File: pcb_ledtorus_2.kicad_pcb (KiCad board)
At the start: 4 copper layers, 199 x 199 mm, 273 parts, among them P1 CONN_02X04, P2 CONN_6, P3 MICRO-SD, P4 CONN_2, P5 KNUSB, P6 CONN_12, U1 STM32F46X_LQFP176, U10 TLC5955, U11 TLC5955, U12 TLC5955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

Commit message: Couple small tweaks, 3d shapes.
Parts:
- X1: footprint knielsenlib_old:2-SOJ -> knielsenlib:2-SOJ
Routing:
- net /LEDs/sclk2: track 0.00 -> 34.0 mm
- net /LEDs/gsclk2: track 0.00 -> 33.9 mm
- net Net-(U6-Pad28): track 0.00 -> 18.0 mm
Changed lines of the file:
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@@
   (general
     (links 1069)
-    (no_connects 979)
+    (no_connects 976)
     (area 50.449846 50.424999 249.550154 249.575001)
     (thickness 0.8)
     (drawings 85)
-    (tracks 3)
+    (tracks 14)
     (zones 0)
     (modules 273)
@@
     (uvia_drill 0.127)
   )
+  (module knielsenlib:TO-252-3 (layer B.Cu)
+    (at 127.286 215.22072)
+    (descr "TO-252-3 (also PFM) package")
+    (fp_text reference U3 (at 0 7.69874) (layer B.SilkS)
+      (effects (font (thickness 0.3048)) (justify mirror))
+    )
+    (fp_text value LP38691 (at 0 -5.99948) (layer B.SilkS)
+      (effects (font (thickness 0.3048)) (justify mirror))
+    )
+    (pad 1 smd rect (at -2.286 -3.22072) (size 1.30048 1.69926) (layers B.Cu B.Paste B.Mask)
+      (net 3 +3V3))
+    (pad 3 smd rect (at 2.286 -3.22072) (size 1.30048 1.69926) (layers B.Cu B.Paste B.Mask)
+      (net 6 +5V))
+    (pad 2 smd rect (at 0 3.22072) (size 5.4991 5.69976) (layers B.Cu B.Paste B.Mask)
+      (net 2 GND))
+    (model TO_SOT_Packages_SMD.3dshapes/TO-252-2Lead.wrl
+      (at (xyz 0 -0.118 0))
+      (scale (xyz 1 1 1))
+      (rotate (xyz 0 0 0))
+    )
+  )
+  (module knielsenlib:RGB_0603 (layer F.Cu)
+    (at 199.734424 109.343679 90)
+    (descr "RGB led, 0603")
+    (fp_text reference LD35 (at 0 -1.15 90) (layer F.SilkS)
+      (effects (font (size 0.20066 0.20066) (thickness 0.04064)))
+    )
+    (fp_text value RGB_LED_SMALL (at 0 1.15 90) (layer F.SilkS) hide
+      (effects (font (size 0.20066 0.20066) (thickness 0.04064)))
+    )
+    (fp_line (start 1.75 -0.1) (end 1.75 0.1) (layer F.SilkS) (width 0.15))
+    (fp_line (start -0.8 -0.55) (end -0.8 -0.75) (layer F.SilkS) (width 0.15))
+    (fp_line (start -0.8 0.25) (end -0.8 -0.25) (layer F.SilkS) (width 0.15))
+    (fp_line (start -0.8 0.75) (end -0.8 0.55) (layer F.SilkS) (width 0.15))
+    (fp_line (start 0.8 0.55) (end 0.8 0.75) (layer F.SilkS) (width 0.15))
+    (fp_line (start 0.8 -0.25) (end 0.8 0.25) (layer F.SilkS) (width 0.15))
+    (fp_line (start 0.8 -0.75) (end 0.8 -0.55) (layer F.SilkS) (width 0.15))
+    (fp_arc (start 0.95 -0.4) (end 0.8 -0.25) (angle 90) (layer F.SilkS) (width 0.15))
+    (fp_arc (start 0.95 0.4) (end 0.8 0.55) (angle 90) (layer F.SilkS) (width 0.15))
+    (fp_arc (start -0.95 0.4) (end -0.8 0.25) (angle 90) (layer F.SilkS) (width 0.15))
+    (fp_arc (start -0.95 -0.4) (end -0.8 -0.55) (angle 90) (layer F.SilkS) (width 0.15))
+    (fp_line (start -0.8 -0.75) (end 0.8 -0.75) (layer F.SilkS) (width 0.15))
+    (fp_line (start 0.8 0.75) (end -0.8 0.75) (layer F.SilkS) (width 0.15))
+    (pad 4 smd rect (at 0.875 -0.4625 90) (size 1.05 0.575) (layers F.Cu F.Paste F.Mask)
+      (net 118 /LEDs/led35b))
+    (pad 1 smd rect (at 0.875 0.4625 90) (size 1.05 0.575) (layers F.Cu F.Paste F.Mask)
+      (net 6 +5V))
+    (pad 2 smd rect (at -0.875 0.4625 90) (size 1.05 0.575) (layers F.Cu F.Paste F.Mask)
+      (net 119 /LEDs/led35r))
+    (pad 3 smd rect (at -0.875 -0.4625 90) (size 1.05 0.575) (layers F.Cu F.Paste F.Mask)
+      (net 120 /LEDs/led35g))
+    (model walter/smd_leds/led_0603.wrl
+      (at (xyz 0 0 0))
+      (scale (xyz 1 1 1))
+      (rotate (xyz 0 0 0))
+    )
+  )
   (module knielsenlib:SWITCH_FSMJSMA (layer B.Cu)
     (at 152.5 179.04914)
@@
   )
   (module knielsenlib:RGB_0603 (layer F.Cu)
-    (at 199.734424 109.343679 90)
-    (descr "RGB led, 0603")
-    (fp_text reference LD35 (at 0 -1.15 90) (layer F.SilkS)
-      (effects (font (size 0.20066 0.20066) (thickness 0.04064)))
-    )
-    (fp_text value RGB_LED_SMALL (at 0 1.15 90) (layer F.SilkS) hide
-      (effects (font (size 0.20066 0.20066) (thickness 0.04064)))
-    )
-    (fp_line (start 1.75 -0.1) (end 1.75 0.1) (layer F.SilkS) (width 0.15))
-    (fp_line (start -0.8 -0.55) (end -0.8 -0.75) (layer F.SilkS) (width 0.15))
-    (fp_line (start -0.8 0.25) (end -0.8 -0.25) (layer F.SilkS) (width 0.15))
-    (fp_line (start -0.8 0.75) (end -0.8 0.55) (layer F.SilkS) (width 0.15))
-    (fp_line (start 0.8 0.55) (end 0.8 0.75) (layer F.SilkS) (width 0.15))
-    (fp_line (start 0.8 -0.25) (end 0.8 0.25) (layer F.SilkS) (width 0.15))
-    (fp_line (start 0.8 -0.75) (end 0.8 -0.55) (layer F.SilkS) (width 0.15))
-    (fp_arc (start 0.95 -0.4) (end 0.8 -0.25) (angle 90) (layer F.SilkS) (width 0.15))
-    (fp_arc (start 0.95 0.4) (end 0.8 0.55) (angle 90) (layer F.SilkS) (width 0.15))
-    (fp_arc (start -0.95 0.4) (end -0.8 0.25) (angle 90) (layer F.SilkS) (width 0.15))
-    (fp_arc (start -0.95 -0.4) (end -0.8 -0.55) (angle 90) (layer F.SilkS) (width 0.15))
-    (fp_line (start -0.8 -0.75) (end 0.8 -0.75) (layer F.SilkS) (width 0.15))
-    (fp_line (start 0.8 0.75) (end -0.8 0.75) (layer F.SilkS) (width 0.15))
-    (pad 4 smd rect (at 0.875 -0.4625 90) (size 1.05 0.575) (layers F.Cu F.Paste F.Mask)
-      (net 118 /LEDs/led35b))
-    (pad 1 smd rect (at 0.875 0.4625 90) (size 1.05 0.575) (layers F.Cu F.Paste F.Mask)
-      (net 6 +5V))
-    (pad 2 smd rect (at -0.875 0.4625 90) (size 1.05 0.575) (layers F.Cu F.Paste F.Mask)
-      (net 119 /LEDs/led35r))
-    (pad 3 smd rect (at -0.875 -0.4625 90) (size 1.05 0.575) (layers F.Cu F.Paste F.Mask)
-      (net 120 /LEDs/led35g))
-    (model walter/smd_leds/led_0603.wrl
-      (at (xyz 0 0 0))
-      (scale (xyz 1 1 1))
-      (rotate (xyz 0 0 0))
-    )
-  )
-  (module knielsenlib:RGB_0603 (layer F.Cu)
     (at 206.176698 109.343679 90)
     (descr "RGB led, 0603")
@@
     )
   )
-  (module knielsenlib:TO-252-3 (layer B.Cu)
-    (at 127.286 215.22072)
-    (descr "TO-252-3 (also PFM) package")
-    (fp_text reference U3 (at 0 7.69874) (layer B.SilkS)
-      (effects (font (thickness 0.3048)) (justify mirror))
-    )
-    (fp_text value LP38691 (at 0 -5.99948) (layer B.SilkS)
-      (effects (font (thickness 0.3048)) (justify mirror))
-    )
-    (pad 1 smd rect (at -2.286 -3.22072) (size 1.30048 1.69926) (layers B.Cu B.Paste B.Mask)
-      (net 3 +3V3))
-    (pad 3 smd rect (at 2.286 -3.22072) (size 1.30048 1.69926) (layers B.Cu B.Paste B.Mask)
-      (net 6 +5V))
-    (pad 2 smd rect (at 0 3.22072) (size 5.4991 5.69976) (layers B.Cu B.Paste B.Mask)
-      (net 2 GND))
-  )
-  (module knielsenlib_old:2-SOJ (layer B.Cu)
-    (at 104.5 144.4501 90)
-    (descr "Eg. MA-505 crystal")
-    (fp_text reference X1 (at 0 5.00126 90) (layer B.SilkS)
-      (effects (font (thickness 0.3048)) (justify mirror))
-    )
-    (fp_text value MA-505 (at 0 -5.00126 90) (layer B.SilkS)
-      (effects (font (thickness 0.3048)) (justify mirror))
-    )
-    (pad 1 smd rect (at -5.5499 0 90) (size 4.09956 5.6007) (layers B.Cu B.Paste B.Mask)
-      (net 10 /Power/osc_in))
-    (pad 2 smd rect (at 5.5499 0 90) (size 4.09956 5.6007) (layers B.Cu B.Paste B.Mask)
-      (net 11 /Power/osc_out))
-  )
   (module knielsenlib:TLC5955DCA (layer B.Cu)
     (at 163 75)
@@
     )
   )
+  (module knielsenlib:2-SOJ (layer B.Cu)
+    (at 104.5 144.4501 90)
+    (descr "Eg. MA-505 crystal")
+    (fp_text reference X1 (at 0 5.00126 90) (layer B.SilkS)
+      (effects (font (thickness 0.3048)) (justify mirror))
+    )
+    (fp_text value MA-505 (at 0 -5.00126 90) (layer B.SilkS)
+      (effects (font (thickness 0.3048)) (justify mirror))
+    )
+    (pad 1 smd rect (at -5.5499 0 90) (size 4.09956 5.6007) (layers B.Cu B.Paste B.Mask)
+      (net 10 /Power/osc_in))
+    (pad 2 smd rect (at 5.5499 0 90) (size 4.09956 5.6007) (layers B.Cu B.Paste B.Mask)
+      (net 11 /Power/osc_out))
+    (model walter/crystal/crystal_smd_ma-505.wrl
+      (at (xyz 0 0 0))
+      (scale (xyz 1 1 1))
+      (rotate (xyz 0 0 0))
+    )
+  )
   (gr_line (start 214.038448 54.010849) (end 210.571762 50.5) (layer Edge.Cuts) (width 0.15))
   (gr_line (start 217.377214 57.713438) (end 214.038448 54.010849) (layer Edge.Cuts) (width 0.15))
@@
   (segment (start 175.635535 81.364465) (end 175.9 81.1) (width 0.2032) (layer F.Cu) (net 6))
   (via (at 175.9 81.1) (size 0.635) (drill 0.3048) (layers F.Cu B.Cu) (net 6))
+  (segment (start 168.7593 107.1) (end 199.7407 107.1) (width 0.2032) (layer B.Cu) (net 652))
+  (segment (start 199.7407 107.1) (end 200 107.3593) (width 0.2032) (layer B.Cu) (net 652))
+  (segment (start 200 107.3593) (end 200 108.475) (width 0.2032) (layer B.Cu) (net 652))
+  (segment (start 168.5 108.475) (end 168.5 107.3593) (width 0.2032) (layer B.Cu) (net 652))
+  (segment (start 168.5 107.3593) (end 168.7593 107.1) (width 0.2032) (layer B.Cu) (net 652))
+  (segment (start 168.5 101) (end 168.5 102.1157) (width 0.2032) (layer B.Cu) (net 683))
+  (segment (start 168.5 102.1157) (end 168.7843 102.4) (width 0.2032) (layer B.Cu) (net 683))
+  (segment (start 168.7843 102.4) (end 199.7157 102.4) (width 0.2032) (layer B.Cu) (net 683))
+  (segment (start 199.7157 102.4) (end 200 102.1157) (width 0.2032) (layer B.Cu) (net 683))
+  (segment (start 200 102.1157) (end 200 101) (width 0.2032) (layer B.Cu) (net 683))
+  (segment (start 181.5 101) (end 199.5 101) (width 0.2032) (layer B.Cu) (net 738))
   (zone (net 2) (net_name GND) (layer In2.Cu) (hatch edge 0.508)
     (connect_pads (clearance 0.2032))

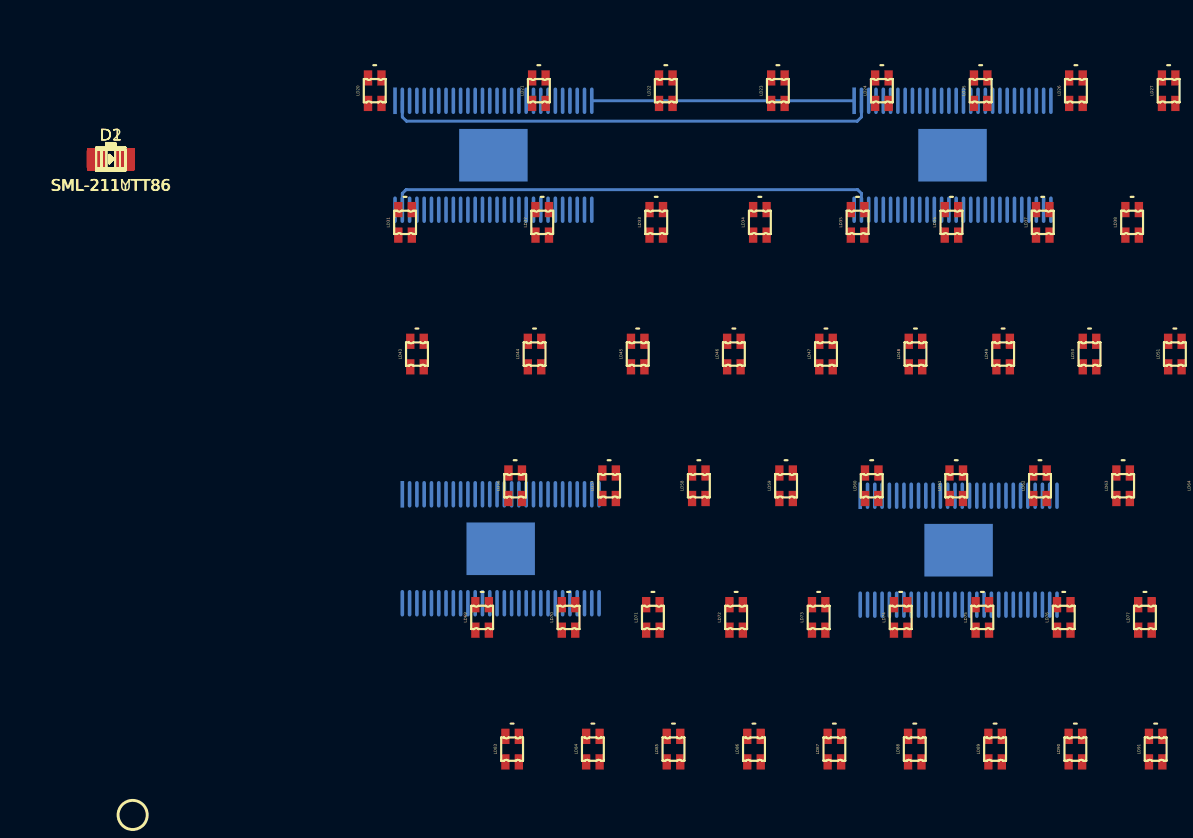
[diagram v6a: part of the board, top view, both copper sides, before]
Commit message: Some experiments with a way to route the LEDs
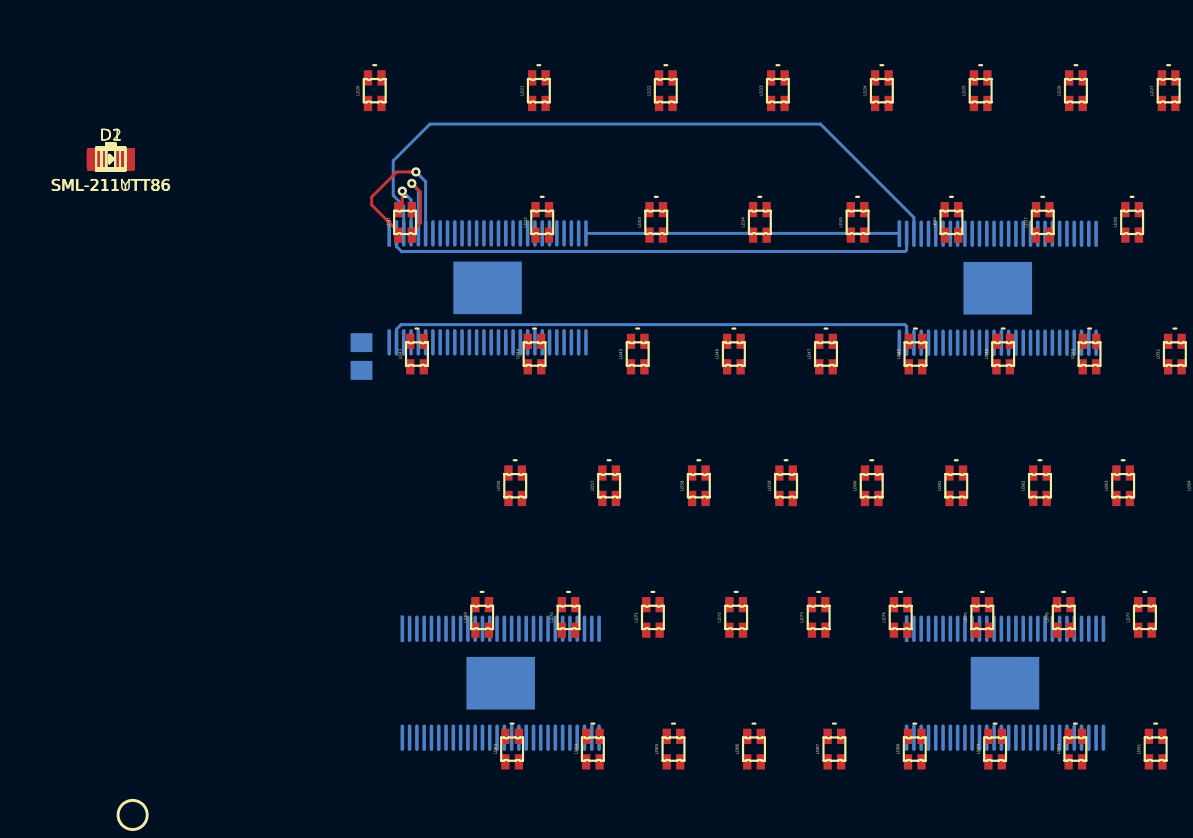
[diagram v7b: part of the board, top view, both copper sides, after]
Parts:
- C36: moved to B.Cu
- moved C36 21.9 mm to (165.7, 118.5), turned to 270 degrees
- moved U9 9.67 mm to (209.8, 141.0)
- moved U7 9.64 mm to (209.3, 113.9)
- moved U8 9.22 mm to (175.2, 141.0)
- moved U6 9.11 mm to (174.3, 113.8)
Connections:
- U5 pad 33: /LEDs/led31g -> /LEDs/led33g
- U5 pad 34: /LEDs/led31r -> /LEDs/led33r
- U5 pad 35: /LEDs/led31b -> /LEDs/led33b
- U6 pad 4: /LEDs/led33b -> /LEDs/led31b
- U6 pad 5: /LEDs/led33r -> /LEDs/led31r
- U6 pad 6: /LEDs/led33g -> /LEDs/led31g
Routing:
- net /LEDs/lat2: track 0.00 -> 45.8 mm
- net /LEDs/led31g: track 0.00 -> 11.6 mm, vias 0 -> 1
- net /LEDs/led31r: track 0.00 -> 7.65 mm, vias 0 -> 1
- net /LEDs/led31b: track 0.00 -> 4.53 mm, vias 0 -> 1
- net Net-(U6-Pad28): track 18.0 -> 21.5 mm
- net /LEDs/gsclk2: track 33.9 -> 37.2 mm
- net /LEDs/sclk2: track 34.0 -> 37.2 mm

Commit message: Intermediate commit
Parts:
- moved U4 7.01 mm to (168.2, 70.3)
- moved U5 4.44 mm to (199.0, 70.3)
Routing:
- net /LEDs/lat3: track 0.00 -> 41.1 mm
- net /LEDs/led96b: track 0.00 -> 37.0 mm, vias 0 -> 1
- net /LEDs/sclk3: track 0.00 -> 36.9 mm
- net /LEDs/gsclk3: track 0.00 -> 36.9 mm
- net /LEDs/led88b: track 0.00 -> 36.1 mm, vias 0 -> 1
- net /LEDs/led96r: track 0.00 -> 35.7 mm, vias 0 -> 1
- net /LEDs/led88r: track 0.00 -> 35.0 mm, vias 0 -> 1
- net /LEDs/led87b: track 0.00 -> 34.5 mm, vias 0 -> 1
- net /LEDs/led87r: track 0.00 -> 33.9 mm, vias 0 -> 1
- net /LEDs/led96g: track 0.00 -> 33.6 mm, vias 0 -> 1
- net /LEDs/led88g: track 0.00 -> 33.1 mm, vias 0 -> 1
- net /LEDs/led87g: track 0.00 -> 31.0 mm, vias 0 -> 1
- net Net-(U8-Pad28): track 0.00 -> 21.1 mm
- net /LEDs/led86r: track 0.00 -> 11.8 mm, vias 0 -> 1
- net /LEDs/led86b: track 0.00 -> 8.81 mm, vias 0 -> 1
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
